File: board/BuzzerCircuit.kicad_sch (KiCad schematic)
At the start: 4 parts, among them Q1 BSS138

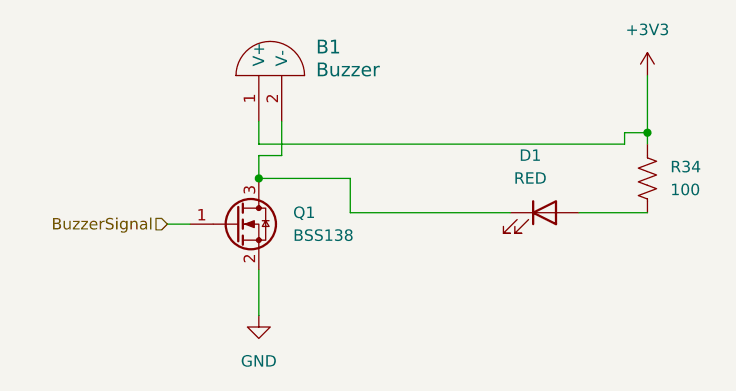
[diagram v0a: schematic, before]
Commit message: added fixes for schematic
redid op amp symbols
put Xs on teensy
Put andersons on current protection page
changed resistor value for buzzer
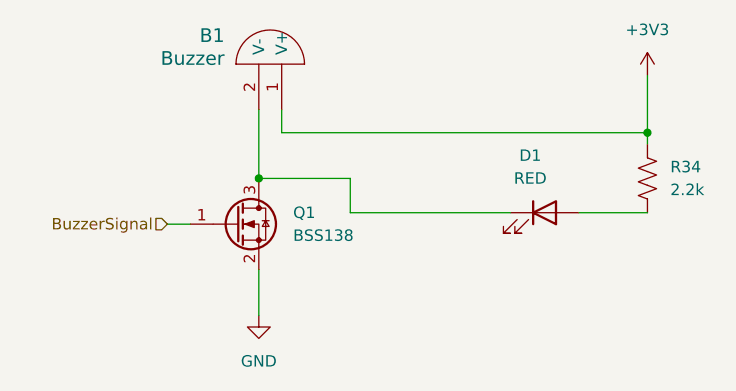
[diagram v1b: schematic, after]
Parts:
- R34: value 100 -> 2.2k
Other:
- moved on the sheet: B1
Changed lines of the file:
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@@
 	(wire
 		(pts
-			(xy 69.85 58.42) (xy 67.31 58.42)
-		)
-		(stroke
-			(width 0)
-			(type default)
-		)
-	)
-	(wire
-		(pts
-			(xy 67.31 57.15) (xy 107.95 57.15)
-		)
-		(stroke
-			(width 0)
-			(type default)
-		)
-	)
-	(wire
-		(pts
-			(xy 107.95 55.88) (xy 110.49 55.88)
+			(xy 69.85 55.88) (xy 110.49 55.88)
 		)
 		(stroke
@@
 	(wire
 		(pts
-			(xy 67.31 58.42) (xy 67.31 60.96)
+			(xy 67.31 53.34) (xy 67.31 60.96)
 		)
 		(stroke
@@
 	(wire
 		(pts
-			(xy 67.31 54.61) (xy 67.31 57.15)
-		)
-		(stroke
-			(width 0)
-			(type default)
-		)
-	)
-	(wire
-		(pts
-			(xy 69.85 54.61) (xy 69.85 58.42)
-		)
-		(stroke
-			(width 0)
-			(type default)
-		)
-	)
-	(wire
-		(pts
-			(xy 107.95 57.15) (xy 107.95 55.88)
+			(xy 69.85 53.34) (xy 69.85 55.88)
 		)
 		(stroke
@@
 	(symbol
 		(lib_id "MRDT_Devices:Buzzer")
-		(at 72.39 49.53 90)
-		(unit 1)
-		(exclude_from_sim no)
-		(in_bom yes)
-		(on_board yes)
-		(dnp no)
-		(fields_autoplaced yes)
+		(at 64.77 48.26 270)
+		(mirror x)
+		(unit 1)
+		(exclude_from_sim no)
+		(in_bom yes)
+		(on_board yes)
+		(dnp no)
 		(property "Reference" "B1"
-			(at 73.66 46.3632 90)
+			(at 63.5 45.0932 90)
 			(effects
 				(font
@@
 		)
 		(property "Value" "Buzzer"
-			(at 73.66 48.9032 90)
+			(at 63.5 47.6332 90)
 			(effects
 				(font
@@
 		)
 		(property "Footprint" ""
-			(at 72.39 49.53 0)
+			(at 64.77 48.26 0)
 			(effects
 				(font
@@
 		)
 		(property "Datasheet" ""
-			(at 72.39 49.53 0)
+			(at 64.77 48.26 0)
 			(effects
 				(font
@@
 		)
 		(property "Description" "Buzzer"
-			(at 72.39 49.53 0)
+			(at 64.77 48.26 0)
 			(effects
 				(font
@@
 			)
 		)
-		(property "Value" "100"
+		(property "Value" "2.2k"
 			(at 113.03 62.2299 0)
 			(effects

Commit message: More footprints added
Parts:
- D1: footprint (none) -> Diode_SMD:D_0603_1608Metric
- R34: footprint (none) -> Resistor_SMD:R_0603_1608Metric
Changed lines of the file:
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@@
 			)
 		)
-		(property "Footprint" ""
+		(property "Footprint" "Diode_SMD:D_0603_1608Metric"
 			(at 99.06 64.77 0)
 			(effects
@@
 			)
 		)
-		(property "Footprint" ""
+		(property "Footprint" "Resistor_SMD:R_0603_1608Metric"
 			(at 111.506 61.214 90)
 			(effects

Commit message: Buzzer Footprint added
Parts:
- B1: footprint (none) -> Buzzer_Beeper:Buzzer_12x9.5RM7.6
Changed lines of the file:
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@@
 			)
 		)
-		(property "Footprint" ""
+		(property "Footprint" "Buzzer_Beeper:Buzzer_12x9.5RM7.6"
 			(at 64.77 48.26 0)
 			(effects

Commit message: Changed footprints to handsolder version
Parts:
- D1: footprint Diode_SMD:D_0603_1608Metric -> LED_SMD:LED_0603_1608Metric_Pad1.05x0.95mm_HandSolder
- R34: footprint Resistor_SMD:R_0603_1608Metric -> Resistor_SMD:R_0603_1608Metric_Pad0.98x0.95mm_HandSolder
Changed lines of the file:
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@@
 			)
 		)
-		(property "Footprint" "Diode_SMD:D_0603_1608Metric"
+		(property "Footprint" "LED_SMD:LED_0603_1608Metric_Pad1.05x0.95mm_HandSolder"
 			(at 99.06 64.77 0)
 			(effects
@@
 			)
 		)
-		(property "Footprint" "Resistor_SMD:R_0603_1608Metric"
+		(property "Footprint" "Resistor_SMD:R_0603_1608Metric_Pad0.98x0.95mm_HandSolder"
 			(at 111.506 61.214 90)
 			(effects

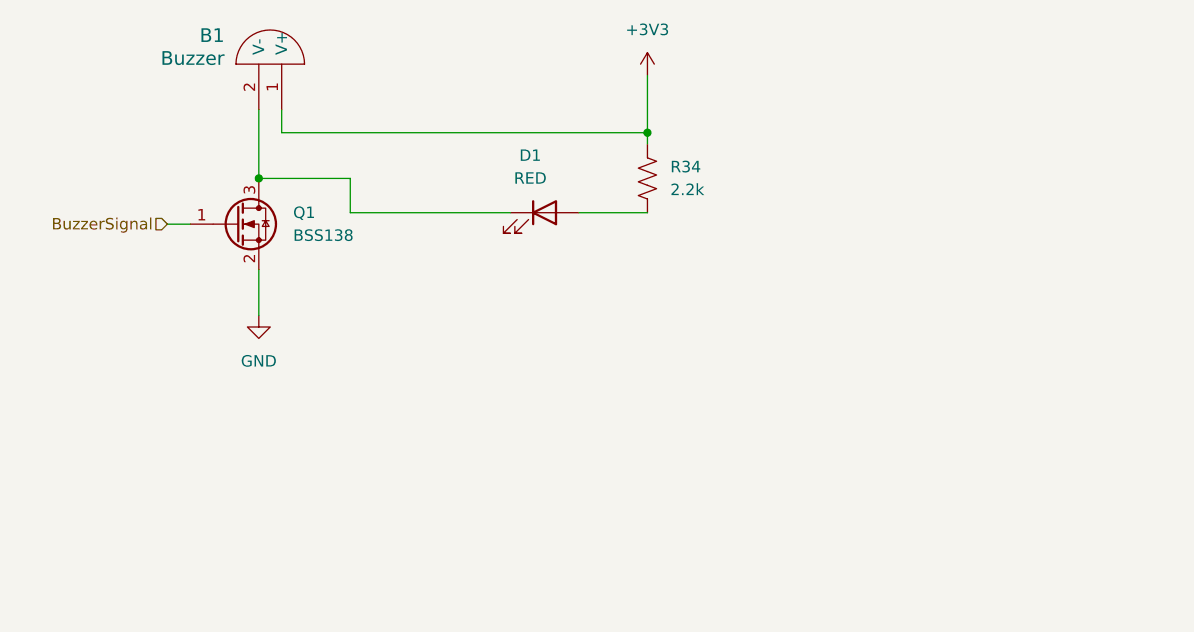
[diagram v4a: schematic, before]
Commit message: Center schematics and layout for prettiness
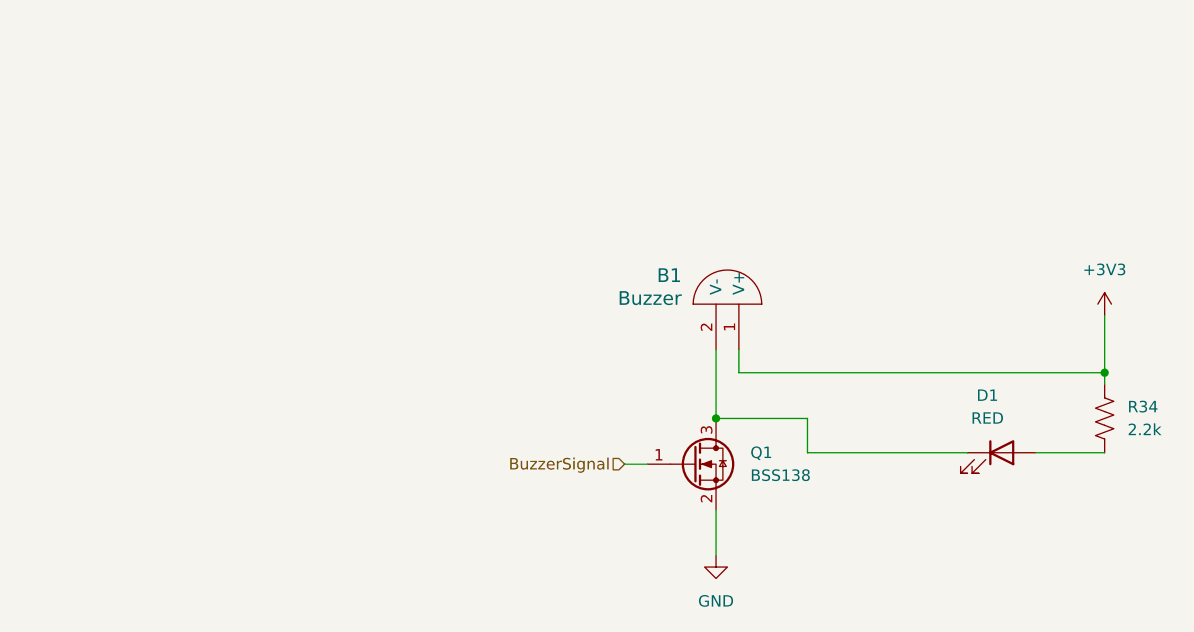
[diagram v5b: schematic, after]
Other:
- moved on the sheet: B1, D1, Q1, R34
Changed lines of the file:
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@@
 	(paper "A4")
 	(junction
-		(at 110.49 55.88)
+		(at 161.29 82.55)
 		(diameter 0)
 		(color 0 0 0 0)
 	)
 	(junction
-		(at 67.31 60.96)
+		(at 118.11 87.63)
 		(diameter 0)
 		(color 0 0 0 0)
@@
 	(wire
 		(pts
-			(xy 77.47 64.77) (xy 77.47 60.96)
-		)
-		(stroke
-			(width 0)
-			(type default)
-		)
-	)
-	(wire
-		(pts
-			(xy 110.49 55.88) (xy 110.49 57.15)
-		)
-		(stroke
-			(width 0)
-			(type default)
-		)
-	)
-	(wire
-		(pts
-			(xy 69.85 55.88) (xy 110.49 55.88)
-		)
-		(stroke
-			(width 0)
-			(type default)
-		)
-	)
-	(wire
-		(pts
-			(xy 110.49 49.53) (xy 110.49 55.88)
-		)
-		(stroke
-			(width 0)
-			(type default)
-		)
-	)
-	(wire
-		(pts
-			(xy 95.25 64.77) (xy 77.47 64.77)
-		)
-		(stroke
-			(width 0)
-			(type default)
-		)
-	)
-	(wire
-		(pts
-			(xy 67.31 71.12) (xy 67.31 76.2)
-		)
-		(stroke
-			(width 0)
-			(type default)
-		)
-	)
-	(wire
-		(pts
-			(xy 77.47 60.96) (xy 67.31 60.96)
-		)
-		(stroke
-			(width 0)
-			(type default)
-		)
-	)
-	(wire
-		(pts
-			(xy 57.15 66.04) (xy 59.69 66.04)
-		)
-		(stroke
-			(width 0)
-			(type default)
-		)
-	)
-	(wire
-		(pts
-			(xy 67.31 53.34) (xy 67.31 60.96)
-		)
-		(stroke
-			(width 0)
-			(type default)
-		)
-	)
-	(wire
-		(pts
-			(xy 102.87 64.77) (xy 110.49 64.77)
-		)
-		(stroke
-			(width 0)
-			(type default)
-		)
-	)
-	(wire
-		(pts
-			(xy 69.85 53.34) (xy 69.85 55.88)
+			(xy 128.27 91.44) (xy 128.27 87.63)
+		)
+		(stroke
+			(width 0)
+			(type default)
+		)
+	)
+	(wire
+		(pts
+			(xy 161.29 82.55) (xy 161.29 83.82)
+		)
+		(stroke
+			(width 0)
+			(type default)
+		)
+	)
+	(wire
+		(pts
+			(xy 120.65 82.55) (xy 161.29 82.55)
+		)
+		(stroke
+			(width 0)
+			(type default)
+		)
+	)
+	(wire
+		(pts
+			(xy 161.29 76.2) (xy 161.29 82.55)
+		)
+		(stroke
+			(width 0)
+			(type default)
+		)
+	)
+	(wire
+		(pts
+			(xy 146.05 91.44) (xy 128.27 91.44)
+		)
+		(stroke
+			(width 0)
+			(type default)
+		)
+	)
+	(wire
+		(pts
+			(xy 118.11 97.79) (xy 118.11 102.87)
+		)
+		(stroke
+			(width 0)
+			(type default)
+		)
+	)
+	(wire
+		(pts
+			(xy 128.27 87.63) (xy 118.11 87.63)
+		)
+		(stroke
+			(width 0)
+			(type default)
+		)
+	)
+	(wire
+		(pts
+			(xy 107.95 92.71) (xy 110.49 92.71)
+		)
+		(stroke
+			(width 0)
+			(type default)
+		)
+	)
+	(wire
+		(pts
+			(xy 118.11 80.01) (xy 118.11 87.63)
+		)
+		(stroke
+			(width 0)
+			(type default)
+		)
+	)
+	(wire
+		(pts
+			(xy 153.67 91.44) (xy 161.29 91.44)
+		)
+		(stroke
+			(width 0)
+			(type default)
+		)
+	)
+	(wire
+		(pts
+			(xy 120.65 80.01) (xy 120.65 82.55)
 		)
 		(stroke
@@
 	(hierarchical_label "BuzzerSignal"
 		(shape input)
-		(at 57.15 66.04 180)
+		(at 107.95 92.71 180)
 		(effects
 			(font
@@
 	(symbol
 		(lib_id "Transistor_FET:BSS138")
-		(at 64.77 66.04 0)
+		(at 115.57 92.71 0)
 		(unit 1)
 		(exclude_from_sim no)
@@
 		(fields_autoplaced yes)
 		(property "Reference" "Q1"
-			(at 71.12 64.7699 0)
+			(at 121.92 91.4399 0)
 			(effects
 				(font
@@
 		)
 		(property "Value" "BSS138"
-			(at 71.12 67.3099 0)
+			(at 121.92 93.9799 0)
 			(effects
 				(font
@@
 		)
 		(property "Footprint" "Package_TO_SOT_SMD:SOT-23"
-			(at 69.85 67.945 0)
+			(at 120.65 94.615 0)
 			(effects
 				(font
@@
 		)
 		(property "Datasheet" "https://www.onsemi.com/pub/Collateral/BSS138-D.PDF"
-			(at 69.85 69.85 0)
+			(at 120.65 96.52 0)
 			(effects
 				(font
@@
 		)
 		(property "Description" "50V Vds, 0.22A Id, N-Channel MOSFET, SOT-23"
-			(at 64.77 66.04 0)
+			(at 115.57 92.71 0)
 			(effects
 				(font
@@
 	(symbol
 		(lib_id "MRDT_Devices:Buzzer")
-		(at 64.77 48.26 270)
+		(at 115.57 74.93 270)
 		(mirror x)
 		(unit 1)
@@
 		(dnp no)
 		(property "Reference" "B1"
-			(at 63.5 45.0932 90)
+			(at 114.3 71.7632 90)
 			(effects
 				(font
@@
 		)
 		(property "Value" "Buzzer"
-			(at 63.5 47.6332 90)
+			(at 114.3 74.3032 90)
 			(effects
 				(font
@@
 		)
 		(property "Footprint" "Buzzer_Beeper:Buzzer_12x9.5RM7.6"
-			(at 64.77 48.26 0)
+			(at 115.57 74.93 0)
 			(effects
 				(font
@@
 		)
 		(property "Datasheet" ""
-			(at 64.77 48.26 0)
+			(at 115.57 74.93 0)
 			(effects
 				(font
@@
 		)
 		(property "Description" "Buzzer"
-			(at 64.77 48.26 0)
+			(at 115.57 74.93 0)
 			(effects
 				(font
@@
 	(symbol
 		(lib_id "power:+3V3")
-		(at 110.49 49.53 0)
+		(at 161.29 76.2 0)
 		(unit 1)
 		(exclude_from_sim no)
@@
 		(fields_autoplaced yes)
 		(property "Reference" "#PWR01"
-			(at 110.49 53.34 0)
+			(at 161.29 80.01 0)
 			(effects
 				(font
@@
 		)
 		(property "Value" "+3V3"
-			(at 110.49 44.45 0)
+			(at 161.29 71.12 0)
 			(effects
 				(font
@@
 		)
 		(property "Footprint" ""
-			(at 110.49 49.53 0)
+			(at 161.29 76.2 0)
 			(effects
 				(font
@@
 		)
 		(property "Datasheet" ""
-			(at 110.49 49.53 0)
+			(at 161.29 76.2 0)
 			(effects
 				(font
@@
 		)
 		(property "Description" "Power symbol creates a global label with name \"+3V3\""
-			(at 110.49 49.53 0)
+			(at 161.29 76.2 0)
 			(effects
 				(font
@@
 	(symbol
 		(lib_id "Device:LED")
-		(at 99.06 64.77 0)
+		(at 149.86 91.44 0)
 		(unit 1)
 		(exclude_from_sim no)
@@
 		(fields_autoplaced yes)
 		(property "Reference" "D1"
-			(at 97.4725 58.42 0)
+			(at 148.2725 85.09 0)
 			(effects
 				(font
@@
 		)
 		(property "Value" "RED"
-			(at 97.4725 60.96 0)
+			(at 148.2725 87.63 0)
 			(effects
 				(font
@@
 		)
 		(property "Footprint" "LED_SMD:LED_0603_1608Metric_Pad1.05x0.95mm_HandSolder"
-			(at 99.06 64.77 0)
+			(at 149.86 91.44 0)
 			(effects
 				(font
@@
 		)
 		(property "Datasheet" "~"
-			(at 99.06 64.77 0)
+			(at 149.86 91.44 0)
 			(effects
 				(font
@@
 		)
 		(property "Description" "Light emitting diode"
-			(at 99.06 64.77 0)
+			(at 149.86 91.44 0)
 			(effects
 				(font
@@
 		)
 		(property "Sim.Pins" "1=K 2=A"
-			(at 99.06 64.77 0)
+			(at 149.86 91.44 0)
 			(effects
 				(font
@@
 	(symbol
 		(lib_id "power:GND")
-		(at 67.31 76.2 0)
+		(at 118.11 102.87 0)
 		(unit 1)
 		(exclude_from_sim no)
@@
 		(fields_autoplaced yes)
 		(property "Reference" "#PWR030"
-			(at 67.31 82.55 0)
+			(at 118.11 109.22 0)
 			(effects
 				(font
@@
 		)
 		(property "Value" "GND"
-			(at 67.31 81.28 0)
+			(at 118.11 107.95 0)
 			(effects
 				(font
@@
 		)
 		(property "Footprint" ""
-			(at 67.31 76.2 0)
+			(at 118.11 102.87 0)
 			(effects
 				(font
@@
 		)
 		(property "Datasheet" ""
-			(at 67.31 76.2 0)
+			(at 118.11 102.87 0)
 			(effects
 				(font
@@
 		)
 		(property "Description" "Power symbol creates a global label with name \"GND\" , ground"
-			(at 67.31 76.2 0)
+			(at 118.11 102.87 0)
 			(effects
 				(font
@@
 	(symbol
 		(lib_id "Device:R_US")
-		(at 110.49 60.96 0)
+		(at 161.29 87.63 0)
 		(unit 1)
 		(exclude_from_sim no)
@@
 		(fields_autoplaced yes)
 		(property "Reference" "R34"
-			(at 113.03 59.6899 0)
+			(at 163.83 86.3599 0)
 			(effects
 				(font
@@
 		)
 		(property "Value" "2.2k"
-			(at 113.03 62.2299 0)
+			(at 163.83 88.8999 0)
 			(effects
 				(font
@@
 		)
 		(property "Footprint" "Resistor_SMD:R_0603_1608Metric_Pad0.98x0.95mm_HandSolder"
-			(at 111.506 61.214 90)
+			(at 162.306 87.884 90)
 			(effects
 				(font
@@
 		)
 		(property "Datasheet" "~"
-			(at 110.49 60.96 0)
+			(at 161.29 87.63 0)
 			(effects
 				(font
@@
 		)
 		(property "Description" "Resistor, US symbol"
-			(at 110.49 60.96 0)
-			(effects
-				(font
+			(at 161.29 87.63 0)
+			(effects
+				(font

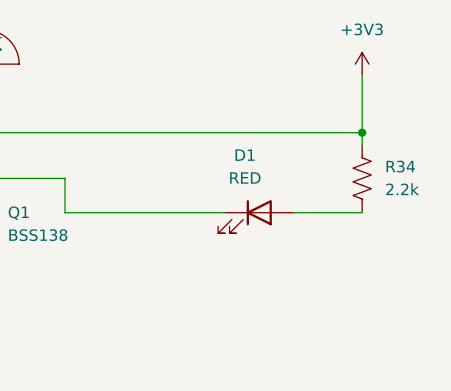
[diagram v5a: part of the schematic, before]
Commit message: add label for battery sensing molex connector
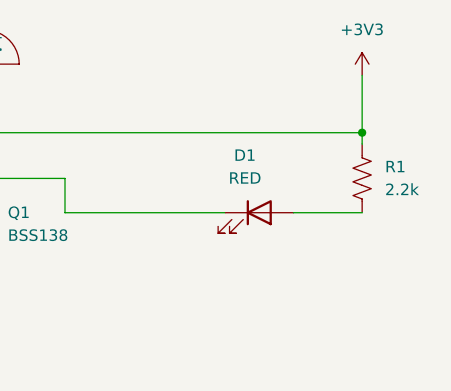
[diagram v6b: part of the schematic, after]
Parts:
- renumbered R34 to R1
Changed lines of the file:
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@@
 		(dnp no)
 		(fields_autoplaced yes)
-		(property "Reference" "R34"
+		(property "Reference" "R1"
 			(at 163.83 86.3599 0)
 			(effects
@@
 			(project ""
 				(path "/7eaa639d-7062-45e7-be05-1c2855431307/e47a1f56-bf0f-4422-8cc9-80190c585d1d"
-					(reference "R34")
+					(reference "R1")
 					(unit 1)
 				)
